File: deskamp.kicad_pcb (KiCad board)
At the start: 2 copper layers, 34 parts, among them J1 Input 01, J10 Input Select, J2 Input 02, J3 Preamp Out, J5 LFE, J6 Mute, J7 Sleep, J8 Motor, J9 Power, K1 TQ2-12V, K2 TQ2-12V, K3 TQ2-12V, K4 TQ2-12V, Q1 PN2222A, Q2 PN2222A, Q3 PN2222A, Q4 PN2222A, U1 esp32-wemos-d1-mini, U2 L9110, U3 TSR_1-2433

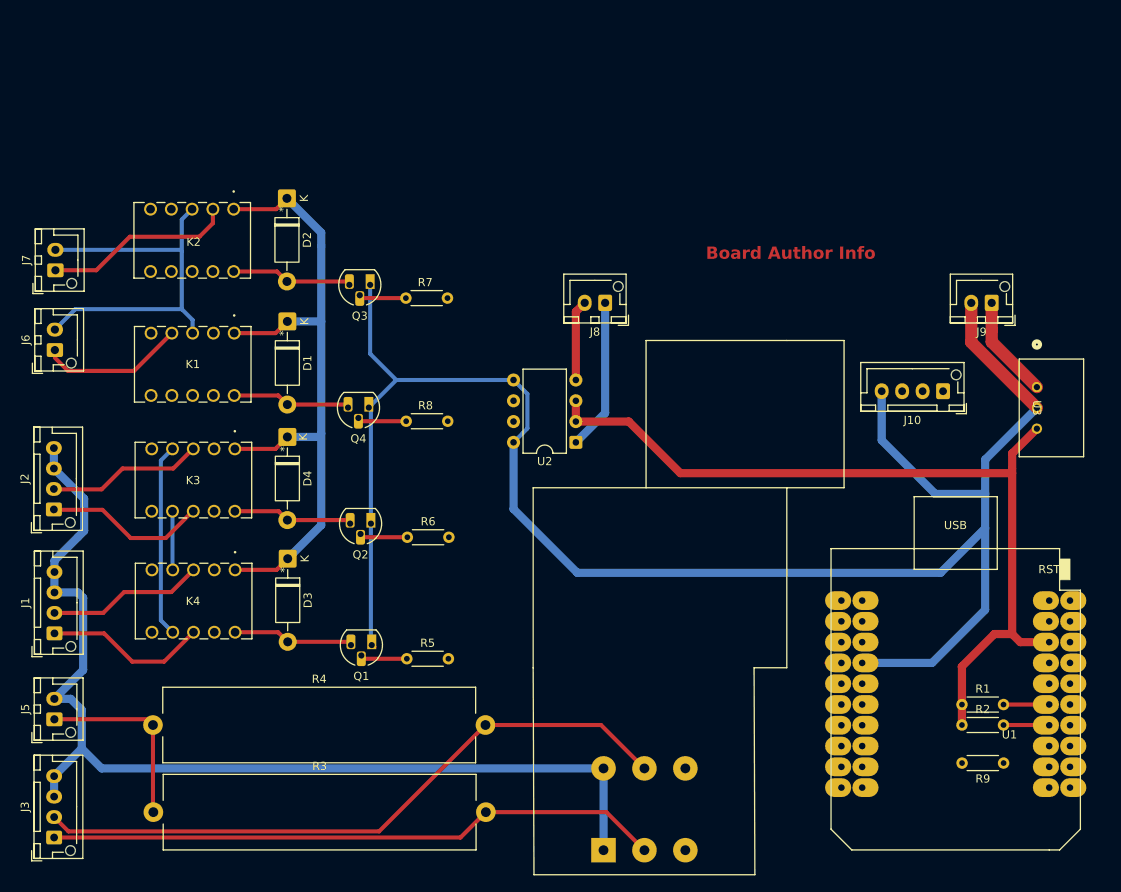
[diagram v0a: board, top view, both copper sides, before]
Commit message: Remove grounds in prep for ground plane
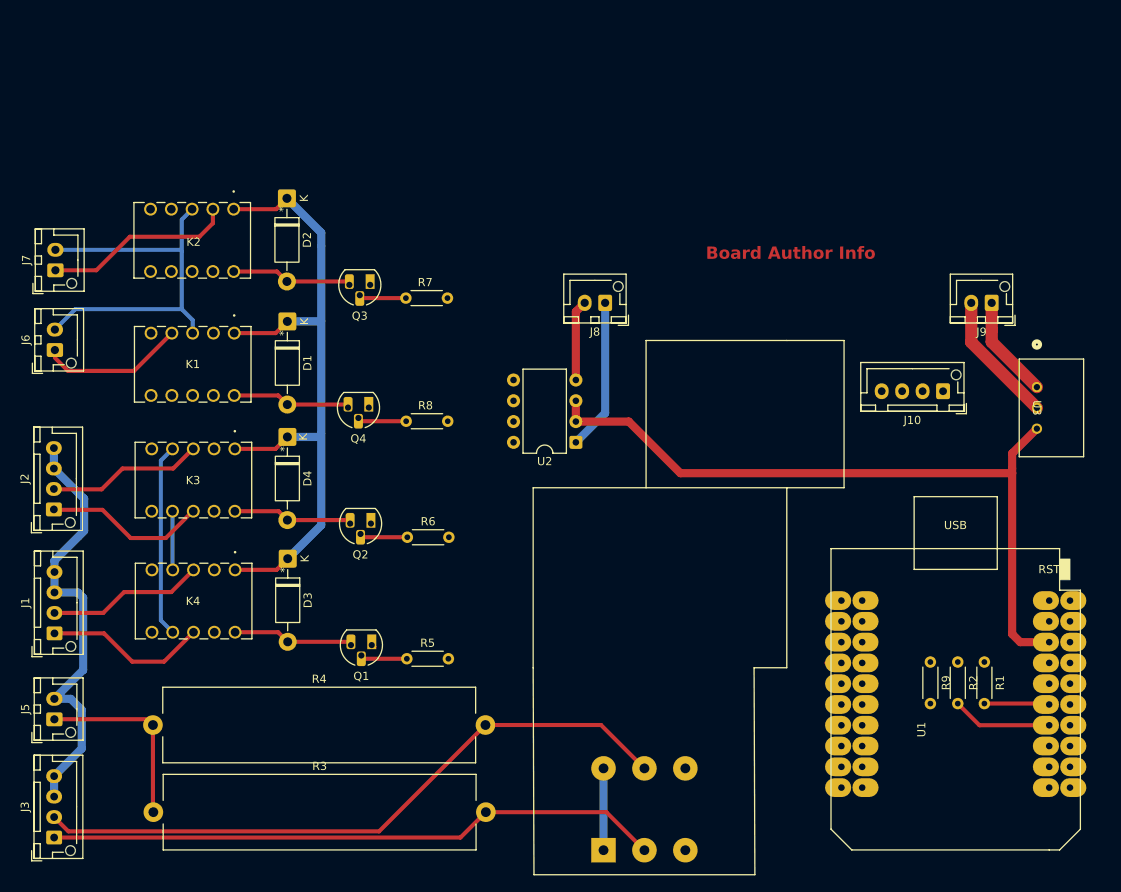
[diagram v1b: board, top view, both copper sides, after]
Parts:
- moved R9 15.3 mm to (169.6, 121.7), turned to -90 degrees
- moved R2 7.72 mm to (172.9, 121.7), turned to -90 degrees
- moved R1 5.88 mm to (176.2, 121.7), turned to -90 degrees
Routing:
- net GND: track 272.4 -> 65.0 mm
- net GNDA: track 129.0 -> 64.2 mm
- net +3V3: track 104.8 -> 89.8 mm
- net Net-(J10-Pin_1): track 5.63 -> 12.3 mm
- net Net-(J10-Pin_3): track 5.82 -> 8.21 mm

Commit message: Ready for ground plane
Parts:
- added REF**: MountingHole_2.2mm_M2_DIN965, MountingHole:MountingHole_2.2mm_M2_DIN965, F.Cu at (189.8, 65.0)
- added REF**: MountingHole_2.2mm_M2_DIN965, MountingHole:MountingHole_2.2mm_M2_DIN965, F.Cu at (102.2, 65.2)
- added REF**: MountingHole_2.2mm_M2_DIN965, MountingHole:MountingHole_2.2mm_M2_DIN965, F.Cu at (69.7, 124.5)
- added REF**: MountingHole_2.2mm_M2_DIN965, MountingHole:MountingHole_2.2mm_M2_DIN965, F.Cu at (152.3, 141.4)
- moved R1 6.53 mm to (172.2, 126.8), turned to 180 degrees
- moved R9 5.64 mm to (172.2, 116.7), turned to 180 degrees
- moved J10 5.06 mm to (171.4, 93.6)
- moved U2 3.98 mm to (129.0, 91.9)
- moved R2 2.74 mm to (172.2, 124.3), turned to 180 degrees
- moved J8 2.70 mm to (132.5, 77.7)
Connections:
- J10 pad 1: Net-(J10-Pin_1) -> GND
- J10 pad 4: GND -> Net-(J10-Pin_4)
- R1 pad 2: Net-(J10-Pin_3) -> Net-(J10-Pin_2)
- R2 pad 2: Net-(J10-Pin_1) -> Net-(J10-Pin_3)
- R5 pad 2: Net-(U1-IO_16/D4) -> Net-(U1-IO_27)
- R6 pad 2: Net-(U1-IO_17/D3) -> Net-(U1-IO_25)
- R7 pad 2: Net-(U1-IO_21/D2/SDA) -> Net-(U1-IO_12/TDI)
- R8 pad 2: Net-(U1-IO_22/D1/SCL) -> Net-(U1-IO_32)
- R9 pad 2: Net-(J10-Pin_2) -> Net-(J10-Pin_4)
- U1 pad 10: Net-(J10-Pin_3) -> unconnected-(U1-IO_19/D6-Pad10)
- U1 pad 24: unconnected-(U1-IO_27-Pad24) -> Net-(U1-IO_27)
- U1 pad 25: Net-(U1-IO_22/D1/SCL) -> unconnected-(U1-IO_22/D1/SCL-Pad25)
- U1 pad 26: unconnected-(U1-IO_25-Pad26) -> Net-(U1-IO_25)
- U1 pad 27: Net-(U1-IO_21/D2/SDA) -> unconnected-(U1-IO_21/D2/SDA-Pad27)
- U1 pad 28: Net-(J10-Pin_2) -> Net-(U1-IO_32)
- U1 pad 29: Net-(U1-IO_17/D3) -> Net-(J10-Pin_2)
- U1 pad 30: unconnected-(U1-IO_12/TDI-Pad30) -> Net-(U1-IO_12/TDI)
- U1 pad 31: Net-(U1-IO_16/D4) -> Net-(J10-Pin_3)
- U1 pad 8: Net-(J10-Pin_1) -> unconnected-(U1-IO_18/D5-Pad8)
- U2 pad 6: Net-(U1-IO_00) -> Net-(U1-IO_04)
- U2 pad 7: Net-(U1-IO_04) -> Net-(U1-IO_00)
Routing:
- net Net-(U1-IO_12/TDI): track 0.00 -> 86.1 mm
- net Net-(U1-IO_04): track 1.50 -> 75.6 mm
- net Net-(K3-Pad7): track 23.6 -> 97.2 mm
- net Net-(U1-IO_32): track 0.00 -> 72.7 mm
- net Net-(K3-Pad4): track 7.18 -> 79.9 mm
- net Net-(U1-IO_00): track 1.84 -> 69.6 mm
- net GNDA: track 64.2 -> 0.00 mm
- net Net-(U1-IO_25): track 0.00 -> 62.4 mm
- net Net-(U1-IO_27): track 0.00 -> 53.5 mm
- net Net-(J10-Pin_2): track 0.00 -> 47.4 mm
- net +3V3: track 89.8 -> 52.5 mm
- net Net-(J10-Pin_3): track 8.21 -> 39.3 mm
- net Net-(J10-Pin_4): track 0.00 -> 25.7 mm
- net Net-(J10-Pin_1): track 12.3 -> 0.00 mm
- net Net-(J8-Pin_1): track 18.5 -> 15.7 mm
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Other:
- board text added: "Passive Preamp almostfinished.me/preamp Rev 1.1"
- board text removed: "Board Author Info"

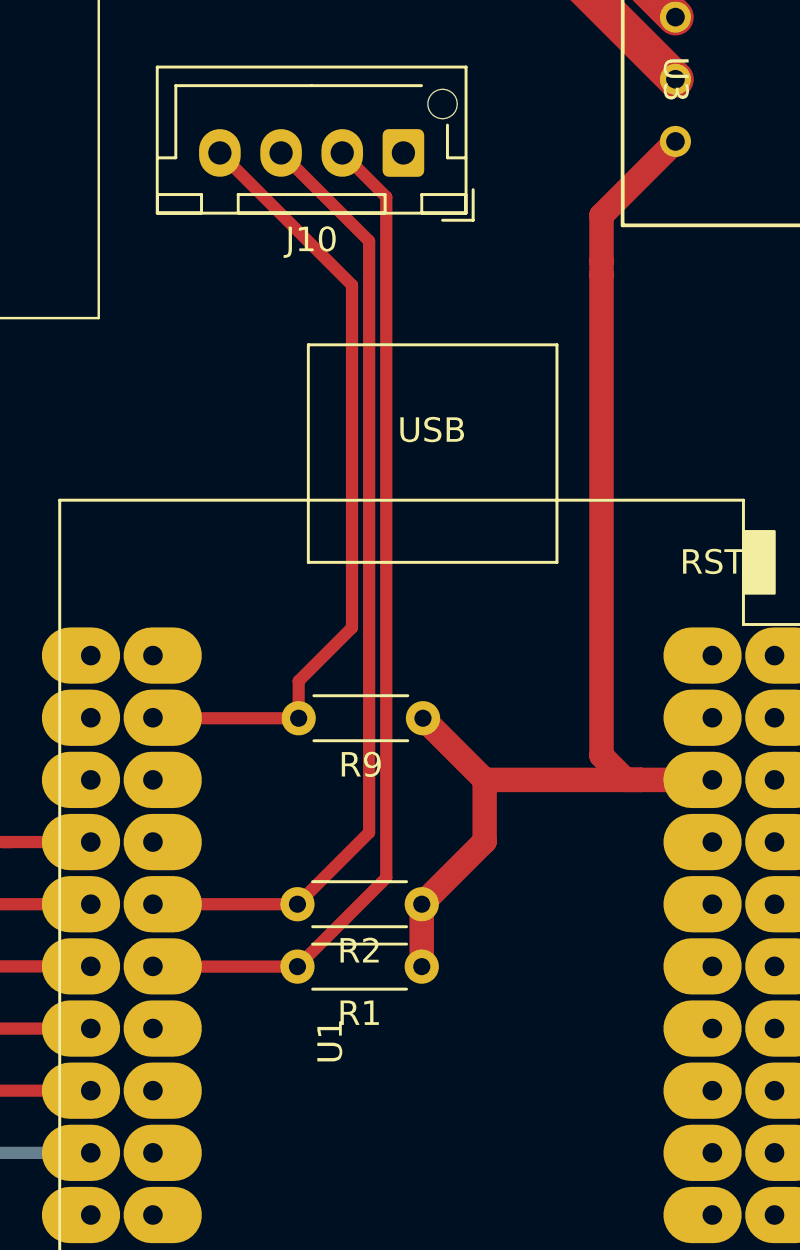
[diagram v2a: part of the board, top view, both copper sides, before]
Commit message: Relocate pullup resistors
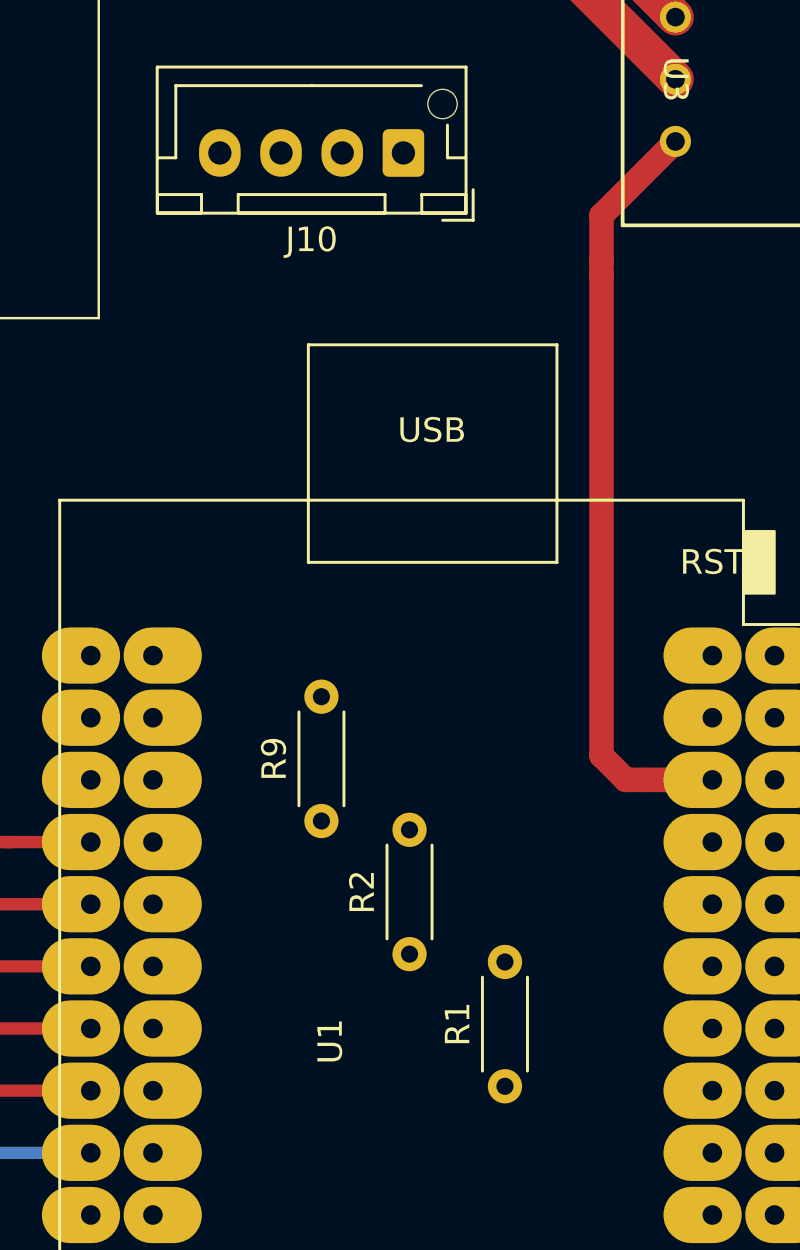
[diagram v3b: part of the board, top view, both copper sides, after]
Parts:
- moved R1 5.96 mm to (175.6, 131.7), turned to 90 degrees
- moved R9 5.90 mm to (168.1, 120.9), turned to 90 degrees
- moved R2 2.10 mm to (171.7, 126.3), turned to 90 degrees
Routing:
- net Net-(J10-Pin_2): track 47.4 -> 0.01 mm
- net Net-(J10-Pin_3): track 39.3 -> 0.00 mm
- net Net-(J10-Pin_4): track 25.7 -> 0.00 mm
- net +3V3: track 52.5 -> 33.8 mm
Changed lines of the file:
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@@
 	(footprint "Resistor_THT:R_Axial_DIN0204_L3.6mm_D1.6mm_P5.08mm_Horizontal"
 		(layer "F.Cu")
-		(at 172.25 116.7 180)
+		(at 168.1 120.9 90)
 		(descr "Resistor, Axial_DIN0204 series, Axial, Horizontal, pin pitch=5.08mm, 0.167W, length*diameter=3.6*1.6mm^2, http://cdn-reichelt.de/documents/datenblatt/B400/1_4W%23YAG.pdf")
 		(tags "Resistor Axial_DIN0204 series Axial Horizontal pin pitch 5.08mm 0.167W length 3.6mm diameter 1.6mm")
 		(property "Reference" "R9"
-			(at 2.54 -1.92 0)
+			(at 2.54 -1.92 90)
 			(layer "F.SilkS")
 			(effects
@@
 		)
 		(property "Value" "10K"
-			(at 2.54 1.92 0)
+			(at 2.54 1.92 90)
 			(layer "F.Fab")
 			(effects
@@
 		)
 		(property "Datasheet" ""
-			(at 0 0 0)
+			(at 0 0 90)
 			(layer "F.Fab")
 			(hide yes)
@@
 		)
 		(property "Description" "Resistor"
-			(at 0 0 0)
+			(at 0 0 90)
 			(layer "F.Fab")
 			(hide yes)
@@
 		(attr through_hole)
 		(fp_line
-			(start 0.62 0.92)
-			(end 4.46 0.92)
+			(start 0.62 -0.92)
+			(end 4.46 -0.92)
 			(stroke
 				(width 0.12)
@@
 		)
 		(fp_line
-			(start 0.62 -0.92)
-			(end 4.46 -0.92)
+			(start 0.62 0.92)
+			(end 4.46 0.92)
 			(stroke
 				(width 0.12)
@@
 		)
 		(fp_text user "${REFERENCE}"
-			(at 2.54 0 0)
+			(at 2.54 0 90)
 			(layer "F.Fab")
 			(effects
@@
 		)
 		(pad "1" thru_hole circle
-			(at 0 0 180)
+			(at 0 0 90)
 			(size 1.4 1.4)
 			(drill 0.7)
@@
 		)
 		(pad "2" thru_hole circle
-			(at 5.08 0 180)
+			(at 5.08 0 90)
 			(size 1.4 1.4)
 			(drill 0.7)
@@
 	(footprint "Resistor_THT:R_Axial_DIN0204_L3.6mm_D1.6mm_P5.08mm_Horizontal"
 		(layer "F.Cu")
-		(at 172.2 126.85 180)
+		(at 175.6 131.74 90)
 		(descr "Resistor, Axial_DIN0204 series, Axial, Horizontal, pin pitch=5.08mm, 0.167W, length*diameter=3.6*1.6mm^2, http://cdn-reichelt.de/documents/datenblatt/B400/1_4W%23YAG.pdf")
 		(tags "Resistor Axial_DIN0204 series Axial Horizontal pin pitch 5.08mm 0.167W length 3.6mm diameter 1.6mm")
 		(property "Reference" "R1"
-			(at 2.54 -1.92 0)
+			(at 2.54 -1.92 90)
 			(layer "F.SilkS")
 			(effects
@@
 		)
 		(property "Value" "10K"
-			(at 2.54 1.92 0)
+			(at 2.54 1.92 90)
 			(layer "F.Fab")
 			(effects
@@
 		)
 		(property "Datasheet" ""
-			(at 0 0 0)
+			(at 0 0 90)
 			(layer "F.Fab")
 			(hide yes)
@@
 		)
 		(property "Description" "Resistor"
-			(at 0 0 0)
+			(at 0 0 90)
 			(layer "F.Fab")
 			(hide yes)
@@
 		(attr through_hole)
 		(fp_line
-			(start 0.62 0.92)
-			(end 4.46 0.92)
+			(start 0.62 -0.92)
+			(end 4.46 -0.92)
 			(stroke
 				(width 0.12)
@@
 		)
 		(fp_line
-			(start 0.62 -0.92)
-			(end 4.46 -0.92)
+			(start 0.62 0.92)
+			(end 4.46 0.92)
 			(stroke
 				(width 0.12)
@@
 		)
 		(fp_text user "${REFERENCE}"
-			(at 2.54 0 0)
+			(at 2.54 0 90)
 			(layer "F.Fab")
 			(effects
@@
 		)
 		(pad "1" thru_hole circle
-			(at 0 0 180)
+			(at 0 0 90)
 			(size 1.4 1.4)
 			(drill 0.7)
@@
 		)
 		(pad "2" thru_hole circle
-			(at 5.08 0 180)
+			(at 5.08 0 90)
 			(size 1.4 1.4)
 			(drill 0.7)
@@
 	(footprint "Resistor_THT:R_Axial_DIN0204_L3.6mm_D1.6mm_P5.08mm_Horizontal"
 		(layer "F.Cu")
-		(at 172.2 124.3 180)
+		(at 171.7 126.34 90)
 		(descr "Resistor, Axial_DIN0204 series, Axial, Horizontal, pin pitch=5.08mm, 0.167W, length*diameter=3.6*1.6mm^2, http://cdn-reichelt.de/documents/datenblatt/B400/1_4W%23YAG.pdf")
 		(tags "Resistor Axial_DIN0204 series Axial Horizontal pin pitch 5.08mm 0.167W length 3.6mm diameter 1.6mm")
 		(property "Reference" "R2"
-			(at 2.54 -1.92 0)
+			(at 2.54 -1.92 90)
 			(layer "F.SilkS")
 			(effects
@@
 		)
 		(property "Value" "10K"
-			(at 2.54 1.92 0)
+			(at 2.54 1.92 90)
 			(layer "F.Fab")
 			(effects
@@
 		)
 		(property "Datasheet" ""
-			(at 0 0 0)
+			(at 0 0 90)
 			(layer "F.Fab")
 			(hide yes)
@@
 		)
 		(property "Description" "Resistor"
-			(at 0 0 0)
+			(at 0 0 90)
 			(layer "F.Fab")
 			(hide yes)
@@
 		(attr through_hole)
 		(fp_line
-			(start 0.62 0.92)
-			(end 4.46 0.92)
+			(start 0.62 -0.92)
+			(end 4.46 -0.92)
 			(stroke
 				(width 0.12)
@@
 		)
 		(fp_line
-			(start 0.62 -0.92)
-			(end 4.46 -0.92)
+			(start 0.62 0.92)
+			(end 4.46 0.92)
 			(stroke
 				(width 0.12)
@@
 		)
 		(fp_text user "${REFERENCE}"
-			(at 2.54 0 0)
+			(at 2.54 0 90)
 			(layer "F.Fab")
 			(effects
@@
 		)
 		(pad "1" thru_hole circle
-			(at 0 0 180)
+			(at 0 0 90)
 			(size 1.4 1.4)
 			(drill 0.7)
@@
 		)
 		(pad "2" thru_hole circle
-			(at 5.08 0 180)
+			(at 5.08 0 90)
 			(size 1.4 1.4)
 			(drill 0.7)
@@
 	)
 	(segment
-		(start 181.15 119.22)
-		(end 174.77 119.22)
-		(width 1)
-		(layer "F.Cu")
-		(net 30)
-	)
-	(segment
-		(start 174.77 119.22)
-		(end 172.25 116.7)
-		(width 1)
-		(layer "F.Cu")
-		(net 30)
-	)
-	(segment
 		(start 180.535 119.22)
 		(end 181.15 119.22)
@@
 	)
 	(segment
-		(start 172.2 116.75)
-		(end 172.25 116.7)
-		(width 0.2)
-		(layer "F.Cu")
-		(net 30)
-	)
-	(segment
 		(start 182.567 93.13)
 		(end 179.545 96.152)
@@
 	)
 	(segment
-		(start 172.2 124.3)
-		(end 172.2 126.85)
-		(width 1)
-		(layer "F.Cu")
-		(net 30)
-	)
-	(segment
-		(start 174.77 119.22)
-		(end 174.77 121.73)
-		(width 1)
-		(layer "F.Cu")
-		(net 30)
-	)
-	(segment
 		(start 128.955 86.83)
 		(end 128.955 89.37)
@@
 	)
 	(segment
-		(start 174.77 121.73)
-		(end 172.2 124.3)
-		(width 1)
-		(layer "F.Cu")
-		(net 30)
-	)
-	(segment
 		(start 179.545 98.57)
 		(end 179.545 118.23)
@@
 	)
 	(segment
-		(start 161.215 124.3)
-		(end 167.12 124.3)
-		(width 0.5)
-		(layer "F.Cu")
-		(net 42)
-	)
-	(segment
-		(start 170.05 97.2)
-		(end 166.45 93.6)
-		(width 0.5)
-		(layer "F.Cu")
-		(net 42)
-	)
-	(segment
-		(start 170.05 121.37)
-		(end 170.05 97.2)
-		(width 0.5)
-		(layer "F.Cu")
-		(net 42)
-	)
-	(segment
-		(start 167.12 124.3)
-		(end 170.05 121.37)
-		(width 0.5)
-		(layer "F.Cu")
-		(net 42)
-	)
-	(segment
 		(start 117.65 111.9)
 		(end 117.65 93.055)
@@
 	)
 	(segment
-		(start 170.75 123.22)
-		(end 170.75 95.4)
-		(width 0.5)
-		(layer "F.Cu")
-		(net 70)
-	)
-	(segment
 		(start 161.225 126.85)
 		(end 161.215 126.84)
@@
 	)
 	(segment
-		(start 167.12 126.85)
-		(end 170.75 123.22)
-		(width 0.5)
-		(layer "F.Cu")
-		(net 70)
-	)
-	(segment
-		(start 167.12 126.85)
-		(end 161.225 126.85)
-		(width 0.5)
-		(layer "F.Cu")
-		(net 70)
-	)
-	(segment
-		(start 167.17 116.7)
-		(end 161.235 116.7)
-		(width 0.5)
-		(layer "F.Cu")
-		(net 70)
-	)
-	(segment
-		(start 170.75 95.4)
-		(end 168.95 93.6)
-		(width 0.5)
-		(layer "F.Cu")
-		(net 70)
-	)
-	(segment
-		(start 161.235 116.7)
-		(end 161.215 116.68)
-		(width 0.2)
-		(layer "F.Cu")
-		(net 70)
-	)
-	(segment
 		(start 183.915 127)
 		(end 184.075 126.84)
@@
 	)
 	(segment
-		(start 169.35 113)
-		(end 167.17 115.18)
-		(width 0.5)
-		(layer "F.Cu")
-		(net 81)
-	)
-	(segment
-		(start 163.95 93.6)
-		(end 169.35 99)
-		(width 0.5)
-		(layer "F.Cu")
-		(net 81)
-	)
-	(segment
-		(start 167.17 115.18)
-		(end 167.17 116.149)
-		(width 0.5)
-		(layer "F.Cu")
-		(net 81)
-	)
-	(segment
-		(start 169.35 99)
-		(end 169.35 113)
-		(width 0.5)
+		(start 161.235 116.7)
+		(end 161.215 116.68)
+		(width 0.2)
 		(layer "F.Cu")
-		(net 81)
+		(net 82)
 	)
 	(embedded_fonts no)

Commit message: Filled zones fun
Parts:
- moved R1 6.93 mm to (170.7, 126.8), turned to 180 degrees
- moved R9 4.94 mm to (170.7, 116.7), turned to 180 degrees
- moved REF** 3.11 mm to (99.9, 67.3)
- moved R2 2.25 mm to (170.7, 124.3), turned to 180 degrees
- moved REF** 2.22 mm to (189.5, 67.2)
- moved J10 1.27 mm to (172.4, 92.8)
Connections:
- U1 pad 37: unconnected-(U1-TD0-Pad37) -> Net-(J10-Pin_4)
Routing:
- net GND: track 65.0 -> 42.2 mm
- net +3V3: track 33.8 -> 54.0 mm
- net Net-(J10-Pin_2): track 0.01 -> 4.48 mm
- net Net-(J10-Pin_3): track 0.00 -> 4.44 mm
- net Net-(J10-Pin_4): track 0.00 -> 4.41 mm
- net Net-(K3-Pad7): track 97.2 -> 100.6 mm
- net Net-(K3-Pad4): track 79.9 -> 81.0 mm
- added copper zone on B.Cu, net GND
- added copper zone on B.Cu, net GNDA
